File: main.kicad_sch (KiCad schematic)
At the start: 150 parts, among them SW1 SW_Push, SW10 SW_Push, SW11 SW_Push, SW12 SW_Push, SW13 SW_Push, SW14 SW_Push, SW15 SW_Push, SW16 SW_Push, SW17 SW_Push, SW18 SW_Push, SW19 SW_Push, SW2 SW_Push, SW20 SW_Push, SW21 SW_Push, SW22 SW_Push, SW23 SW_Push, SW24 SW_Push, SW25 SW_Push, SW26 SW_Push, SW27 SW_Push, SW28 SW_Push, SW29 SW_Push, SW3 SW_Push, SW30 SW_Push, SW31 SW_Push, SW32 SW_Push, SW33 SW_Push, SW34 SW_Push, SW35 SW_Push, SW36 SW_Push, SW37 SW_Push, SW38 SW_Push, SW39 SW_Push, SW4 SW_Push, SW40 SW_Push, SW41 SW_Push, SW42 SW_Push, SW43 SW_Push, SW44 SW_Push, SW45 SW_Push, SW46 SW_Push, SW47 SW_Push, SW48 SW_Push, SW49 SW_Push, SW5 SW_Push, SW50 SW_Push, SW51 SW_Push, SW52 SW_Push, SW53 SW_Push, SW54 SW_Push, SW55 SW_Push, SW56 SW_Push, SW57 SW_Push, SW58 SW_Push, SW59 SW_Push, SW6 SW_Push, SW60 SW_Push, SW61 SW_Push, SW62 SW_Push, SW63 SW_Push, SW64 SW_Push, SW65 SW_Push, SW66 SW_Push, SW67 SW_Push, SW68 SW_Push, SW69 SW_Push, SW7 SW_Push, SW70 SW_Push, SW71 SW_Push, SW72 SW_Push, SW73 SW_Push, SW74 SW_Push, SW75 SW_Push, SW8 SW_Push, SW9 SW_Push

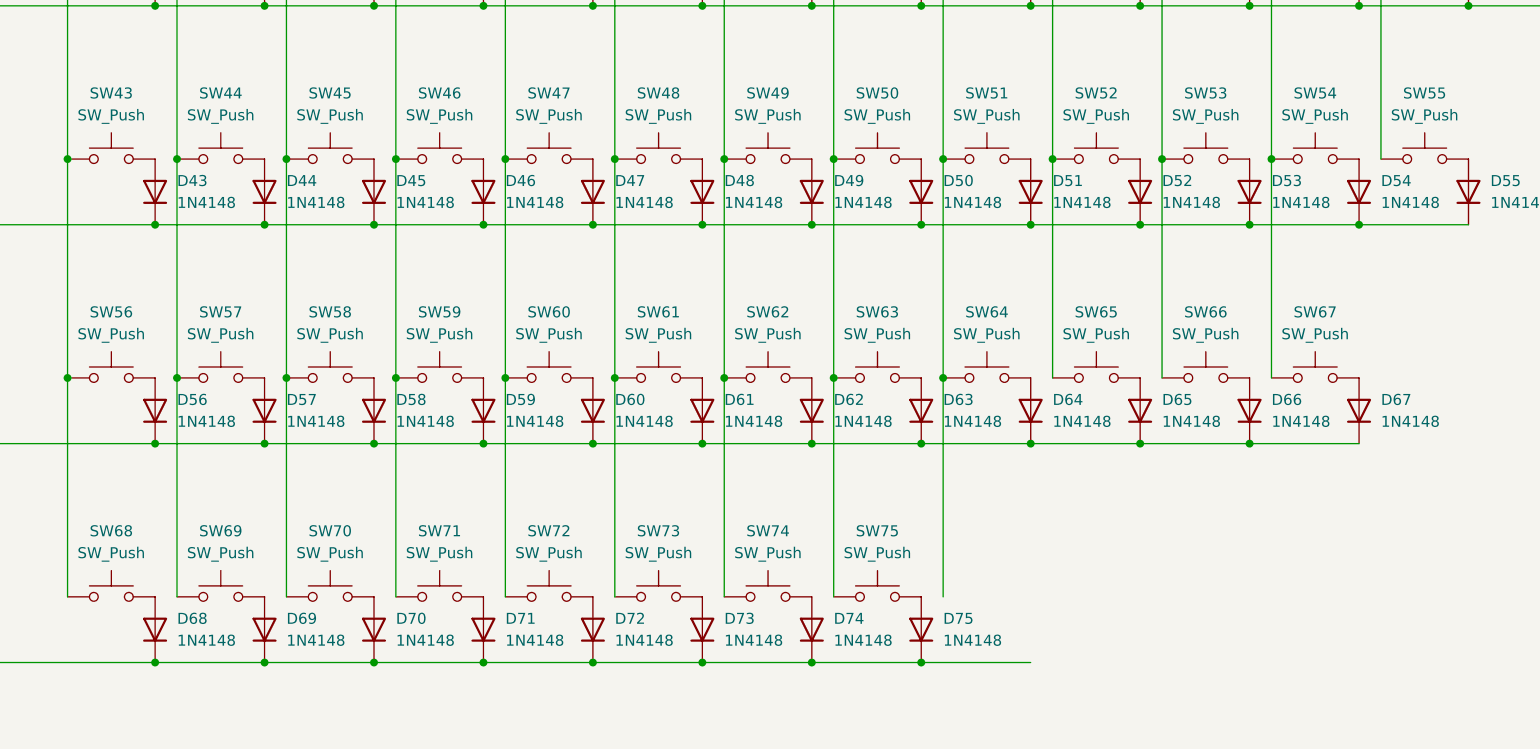
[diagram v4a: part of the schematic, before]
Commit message: Fix routing on Shematic, PCB Diode Place, ROW routing
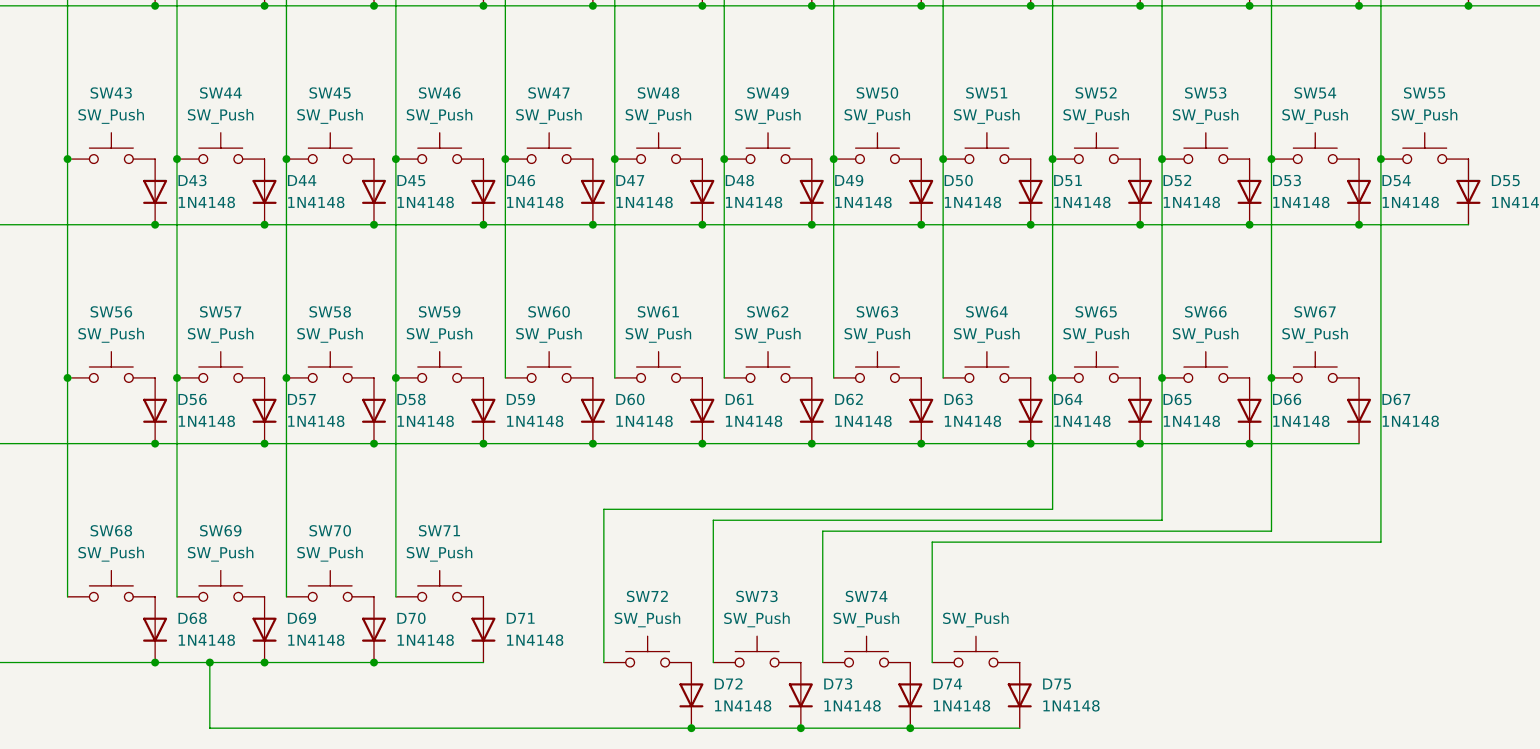
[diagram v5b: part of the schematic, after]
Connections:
- net COL10: now also SW73.1
- net COL11: now also SW74.1
- net COL12: now also SW75.1
- net COL4: no longer SW72.1
- net COL5: no longer SW73.1
- net COL6: no longer SW74.1
- net COL7: no longer SW75.1
- net COL9: now also SW72.1
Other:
- moved on the sheet: D72, D73, D74, D75, SW72, SW73, SW74
